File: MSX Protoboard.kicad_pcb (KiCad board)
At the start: 2 copper layers, 103 x 66 mm, 810 parts

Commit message: Starting routing
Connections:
- ? pad 76: (no net) -> A15
- ? pad 76: (no net) -> A4
- ? pad 76: (no net) -> D2
- ? pad 76: (no net) -> D6
- ? pad 76: (no net) -> A0
- ? pad 76: (no net) -> A6
- ? pad 76: (no net) -> /RD
- ? pad 76: (no net) -> A10
- ? pad 76: (no net) -> A13
- ? pad 76: (no net) -> -12V
- ? pad 76: (no net) -> SW1 (x2)
- ? pad 76: (no net) -> A8
- ? pad 76: (no net) -> D4
- ? pad 76: (no net) -> D0
- ? pad 76: (no net) -> CLOCK
- ? pad 76: (no net) -> A2
- ? pad 76: (no net) -> +12V
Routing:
- net SW1: track 0.00 -> 15.5 mm
- net D6: track 0.00 -> 7.77 mm
- net CLOCK: track 0.00 -> 7.76 mm
- net A2: track 0.00 -> 7.75 mm
- net D4: track 0.00 -> 7.74 mm
- net D2: track 0.00 -> 7.74 mm
- net A13: track 0.00 -> 7.74 mm
- net A4: track 0.00 -> 7.73 mm
- net A15: track 0.00 -> 7.72 mm
- net A0: track 0.00 -> 7.72 mm
- net /RD: track 0.00 -> 7.72 mm
- net A8: track 0.00 -> 7.72 mm
- net D0: track 0.00 -> 7.71 mm
- net A10: track 0.00 -> 7.71 mm
- net +12V: track 0.00 -> 7.70 mm
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
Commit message: V1.0 ready
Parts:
- removed the ? at (66.0, 80.0)
- removed the ? at (76.1, 80.0)
- removed the ? at (142.2, 74.9)
- removed the ? at (73.6, 80.0)
- removed the ? at (71.1, 80.0)
- removed the ? at (68.5, 80.0)
- added ?: , , F.Cu at (71.1, 72.3)
- added ?: , , F.Cu at (81.2, 74.9)
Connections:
- ? pad 76: (no net) -> /M1
- ? pad 76: (no net) -> /RESET
- ? pad 76: (no net) -> +5V (x2)
- ? pad 76: (no net) -> A1
- ? pad 76: (no net) -> D1
- ? pad 76: (no net) -> A9
- ? pad 76: (no net) -> SOUNDIN
- ? pad 76: (no net) -> A14
- ? pad 76: (no net) -> /WAIT
- ? pad 76: (no net) -> /WR
- ? pad 76: (no net) -> A7
- ? pad 76: (no net) -> D7
- ? pad 76: (no net) -> /IORQ
- ? pad 76: (no net) -> A5
- ? pad 76: (no net) -> A3
- ? pad 76: (no net) -> GNDREF (x2)
- ? pad 76: (no net) -> D3
- ? pad 76: (no net) -> D5
- ? pad 76: (no net) -> A12
- ? pad 76: (no net) -> A11
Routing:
- net +5V: track 0.00 -> 24.5 mm
- net GNDREF: track 0.00 -> 24.5 mm
- net D7: track 0.00 -> 11.0 mm
- net A7: track 0.00 -> 11.0 mm
- net /IORQ: track 0.00 -> 11.0 mm
- net D1: track 0.00 -> 11.0 mm
- net /RESET: track 0.00 -> 11.0 mm
- net A14: track 0.00 -> 11.0 mm
- net D5: track 0.00 -> 11.0 mm
- net A1: track 0.00 -> 11.0 mm
- net A11: track 0.00 -> 11.0 mm
- net A12: track 0.00 -> 11.0 mm
- net /M1: track 0.00 -> 11.0 mm
- net SOUNDIN: track 0.00 -> 11.0 mm
- net A5: track 0.00 -> 11.0 mm
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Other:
- board text added: "+12V"
- board text added: "+5V"
- board text added: "-12V"
- board text added: "A0"
- board text added: "A1"
- board text added: "A10"
- board text added: "A11"
- board text added: "A12"
- board text added: "A13"
- board text added: "A14"
- board text added: "A15"
- board text added: "A2"
- board text added: "A3"
- board text added: "A4"
- board text added: "A5"
- board text added: "A6"
- board text added: "A7"
- board text added: "A8"
- board text added: "A9"
- board text added: "BDIR"
- board text added: "CLK"
- board text added: "CS1"
- board text added: "CS12"
- board text added: "CS2"
- board text added: "D0"
- board text added: "D1"
- board text added: "D2"
- board text added: "D3"
- board text added: "D4"
- board text added: "D5"
- board text added: "D6"
- board text added: "D7"
- board text added: "GND"
- board text added: "INT"
- board text added: "IORQ"
- board text added: "M1"
- board text added: "MREQ"
- board text added: "NC"
- board text added: "RCC @ 2022"
- board text added: "RD"
- board text added: "RFSH"
- board text added: "RST"
- board text added: "SLT"
- board text added: "SND"
- board text added: "SW"
- board text added: "WAIT"
- board text added: "WR"
- board text added: "https://github.com/costarc/MSX-Protoboard"
- board text added: "v1.0"

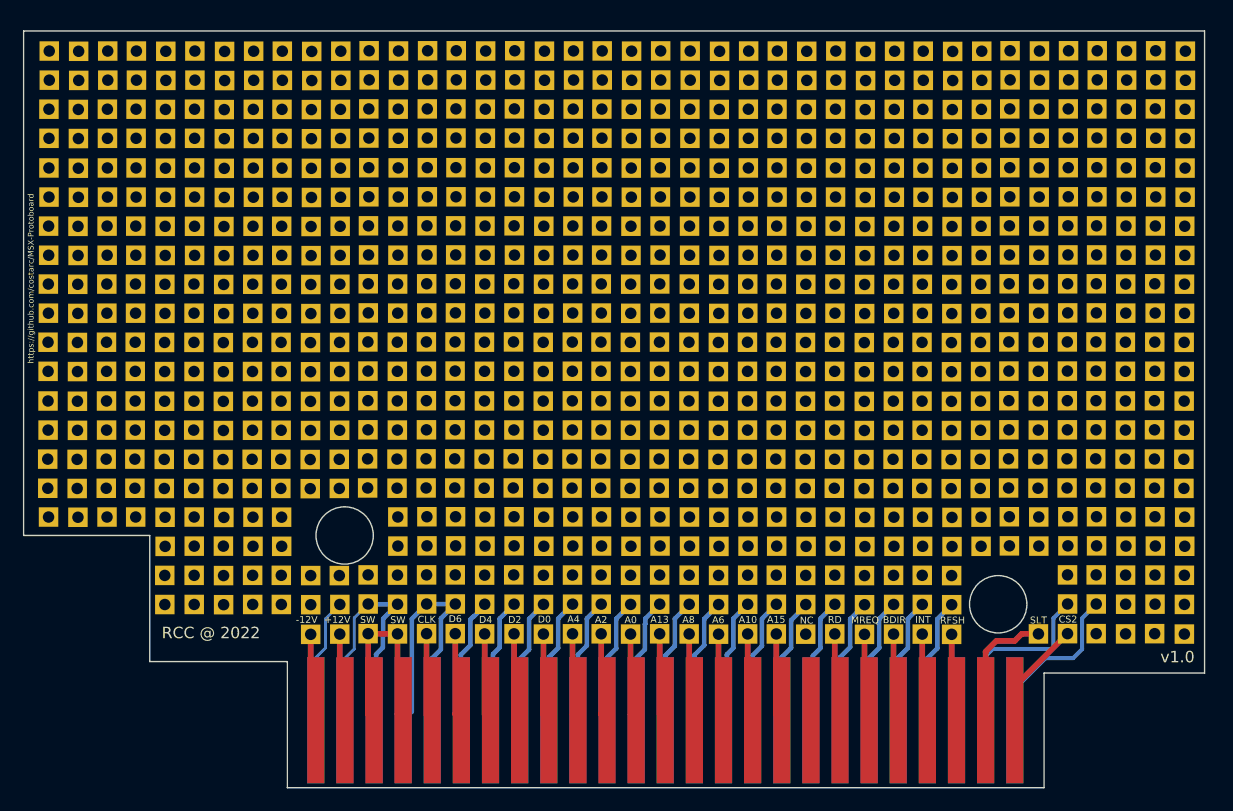
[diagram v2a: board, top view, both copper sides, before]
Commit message: Updated pad SW2 - shorter than SW1. Added fabrication files for V1.0
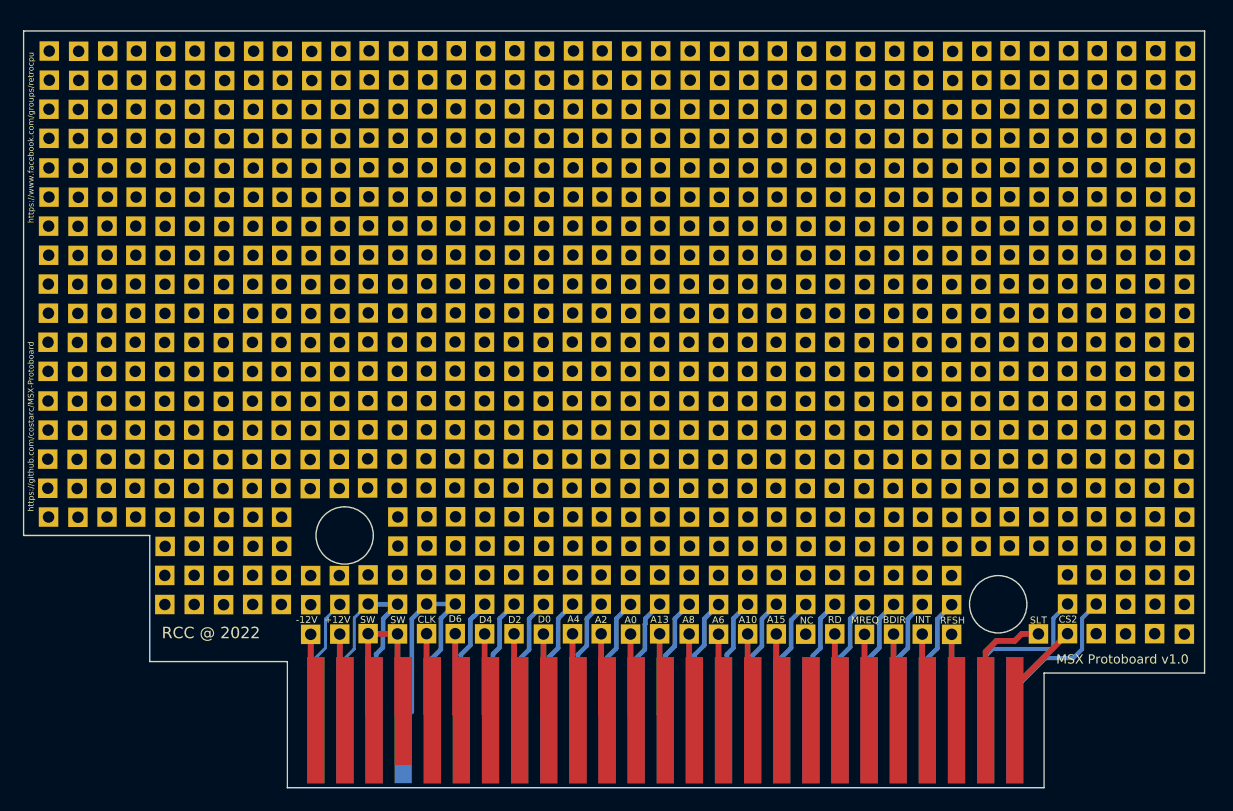
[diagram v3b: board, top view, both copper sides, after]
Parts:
- CONN1: footprint Roni Footprints:MSX_CART -> Roni Footprints:MSX_CART_SW
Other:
- board text added: "MSX Protoboard v1.0"
- board text added: "https://www.facebook.com/groups/retrocpu"
- board text removed: "v1.0"
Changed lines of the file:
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@@
     (pad "76" thru_hole rect (at 0 0 90) (size 1.7 1.7) (drill 1) (layers *.Cu *.Mask))
   )
-  (footprint "Roni Footprints:MSX_CART" (layer "F.Cu")
+  (footprint "Roni Footprints:MSX_CART_SW" (layer "F.Cu")
     (at 103.3244 58.001855)
     (property "Sheetfile" "MSX Protoboard.kicad_sch")
     (property "Sheetname" "")
     (attr through_hole)
-    (fp_text reference "CONN1" (at 6.604 20.32) (layer "F.SilkS") hide
+    (fp_text reference "CONN1" (at 0 -2.54) (layer "F.SilkS") hide
       (effects (font (size 1 1) (thickness 0.15)))
     )
-    (fp_text value "MSX_BUS" (at 6.302025 22.021405) (layer "F.Fab") hide
+    (fp_text value "MSX_BUS" (at 6.302025 22.021405) (layer "F.Fab")
       (effects (font (size 1 1) (thickness 0.15)))
     )
-    (fp_line (start -26.66 35.4) (end 39.34 35.4) (layer "Edge.Cuts") (width 0.12))
-    (fp_line (start -26.66 35.4) (end -26.66 24.4) (layer "Edge.Cuts") (width 0.12))
     (fp_line (start -38.66 13.4) (end -38.66 24.4) (layer "Edge.Cuts") (width 0.12))
-    (fp_line (start 39.34 25.4) (end 39.34 35.4) (layer "Edge.Cuts") (width 0.12))
+    (fp_line (start -26.66 35.4) (end -26.66 24.4) (layer "Edge.Cuts") (width 0.12))
+    (fp_line (start -26.66 35.4) (end 39.34 35.4) (layer "Edge.Cuts") (width 0.12))
+    (fp_line (start 39.34 25.4) (end 53.34 25.4) (layer "Edge.Cuts") (width 0.12))
     (fp_line (start 53.34 -30.6) (end -49.66 -30.6) (layer "Edge.Cuts") (width 0.12))
+    (fp_line (start 39.34 25.4) (end 39.34 35.4) (layer "Edge.Cuts") (width 0.12))
+    (fp_line (start -49.66 13.4) (end -49.66 -30.6) (layer "Edge.Cuts") (width 0.12))
+    (fp_line (start -49.66 13.4) (end -38.66 13.4) (layer "Edge.Cuts") (width 0.12))
     (fp_line (start 53.34 -30.6) (end 53.34 25.4) (layer "Edge.Cuts") (width 0.12))
     (fp_line (start -38.66 24.4) (end -26.66 24.4) (layer "Edge.Cuts") (width 0.12))
-    (fp_line (start -49.66 13.4) (end -38.66 13.4) (layer "Edge.Cuts") (width 0.12))
-    (fp_line (start 39.34 25.4) (end 53.34 25.4) (layer "Edge.Cuts") (width 0.12))
-    (fp_line (start -49.66 13.4) (end -49.66 -30.6) (layer "Edge.Cuts") (width 0.12))
     (fp_circle (center 35.34 19.4) (end 37.84 19.4) (layer "Edge.Cuts") (width 0.12) (fill none))
     (fp_circle (center -21.66 13.4) (end -19.16 13.4) (layer "Edge.Cuts") (width 0.12) (fill none))
@@
     (pad "43" connect rect (at -16.557975 29.514405) (size 1.5 11) (layers "B.Cu" "B.Mask")
       (net 3 "GNDREF") (pinfunction "GND") (pintype "output"))
-    (pad "44" connect rect (at -16.557975 29.514405) (size 1.5 11) (layers "F.Cu" "F.Mask")
+    (pad "44" connect rect (at -16.553954 28.716024) (size 1.50804 9.403238) (layers "F.Cu" "F.Mask")
       (net 47 "SW1") (pinfunction "SW1") (pintype "output"))
     (pad "45" connect rect (at -19.097975 29.514405) (size 1.5 11) (layers "B.Cu" "B.Mask")
@@
     (effects (font (size 0.6 0.6) (thickness 0.125)))
   )
+  (gr_text "https://www.facebook.com/groups/retrocpu" (at 54.3 36.7 90) (layer "F.SilkS")
+    (effects (font (size 0.5 0.5) (thickness 0.125)))
+  )
   (gr_text "SW" (at 86.305676 78.768224) (layer "F.SilkS")
     (effects (font (size 0.6 0.6) (thickness 0.125)))
@@
     (effects (font (size 0.6 0.6) (thickness 0.125)))
   )
-  (gr_text "https://github.com/costarc/MSX-Protoboard" (at 54.3 49 90) (layer "F.SilkS")
+  (gr_text "https://github.com/costarc/MSX-Protoboard" (at 54.3 61.9 90) (layer "F.SilkS")
     (effects (font (size 0.5 0.5) (thickness 0.125)))
   )
@@
     (effects (font (size 0.6 0.6) (thickness 0.125)))
   )
-  (gr_text "v1.0" (at 154.3 82) (layer "F.SilkS")
-    (effects (font (size 1 1) (thickness 0.15)))
+  (gr_text "MSX Protoboard v1.0" (at 149.5 82.2) (layer "F.SilkS")
+    (effects (font (size 0.8 0.8) (thickness 0.15)))
   )
   (gr_text "MREQ" (at 127.04378 78.785773) (layer "F.SilkS")
